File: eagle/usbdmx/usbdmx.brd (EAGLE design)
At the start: 100 x 80 mm, 16 parts, among them IC1 MAX3468CSA, IC2 MAX3468CSA, Q1 16MHz

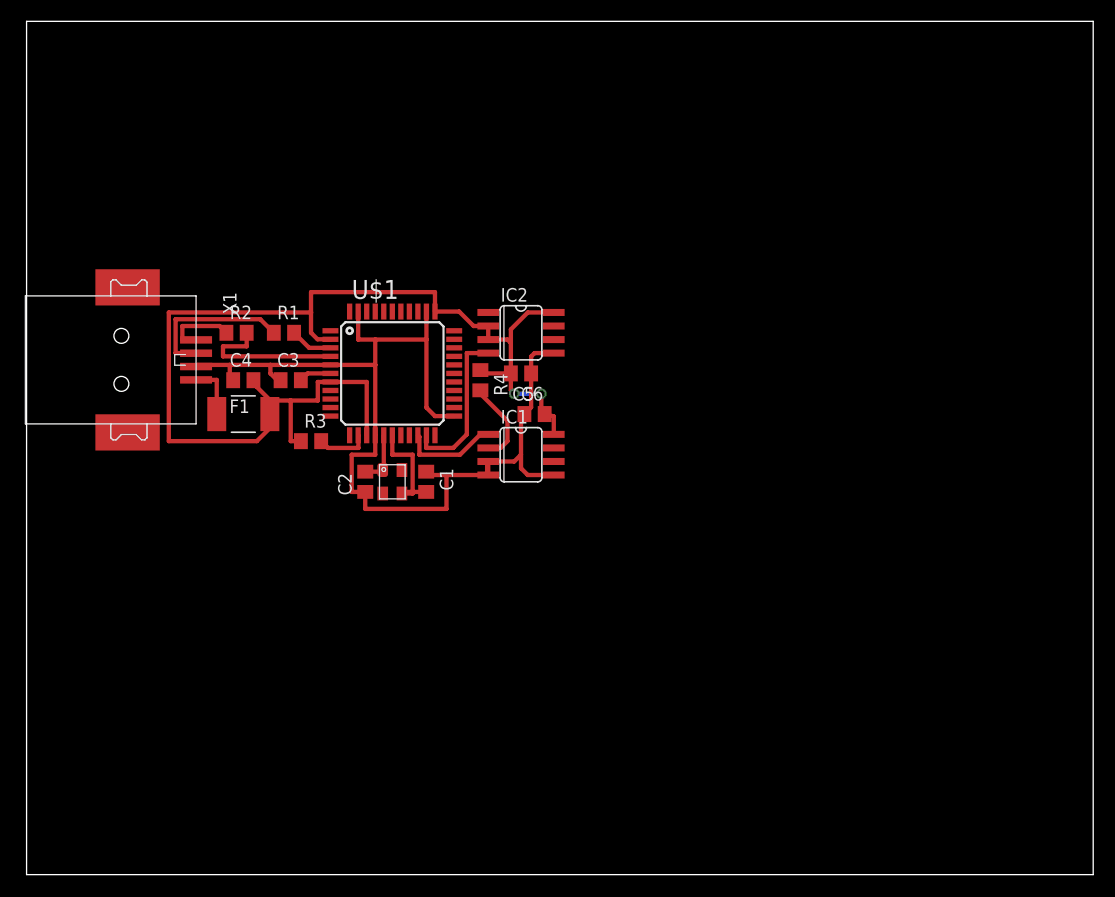
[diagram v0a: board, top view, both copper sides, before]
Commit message: simple layout without galvanic isolation
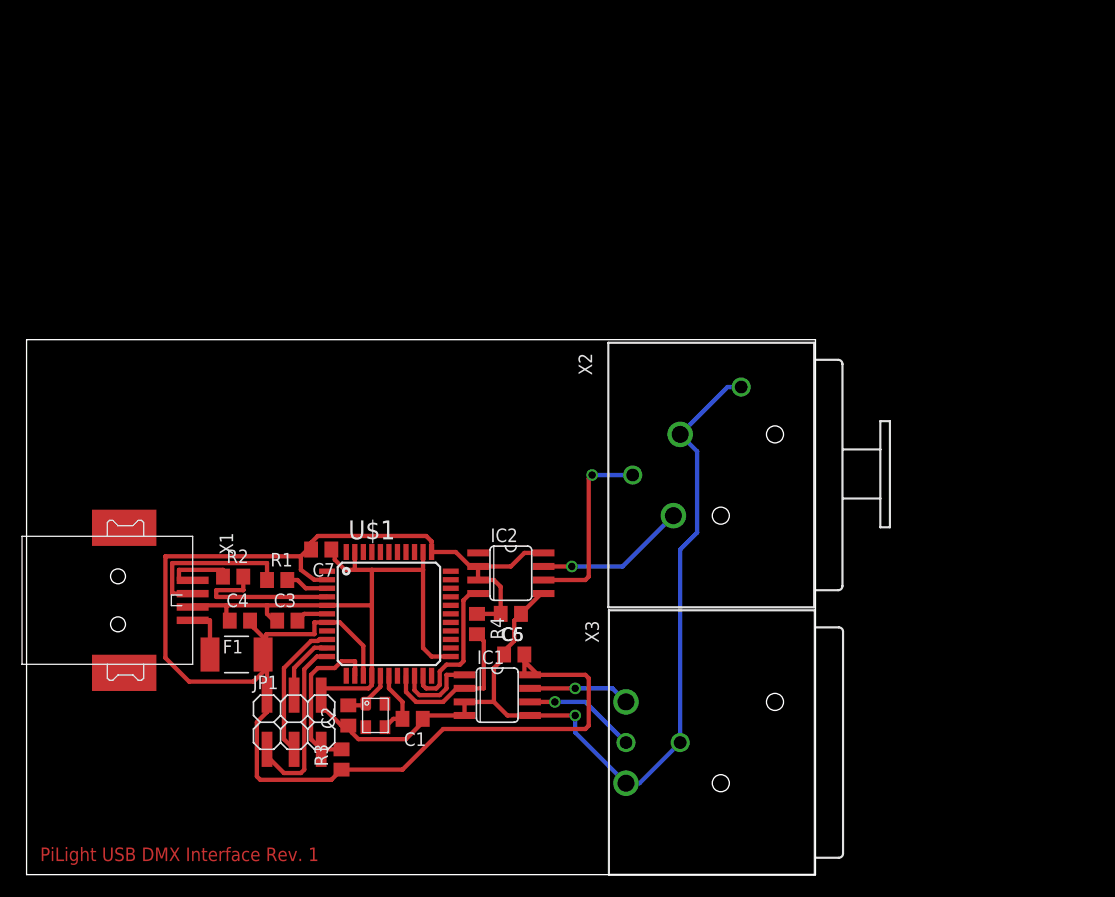
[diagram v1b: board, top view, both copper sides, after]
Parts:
- added C7: (no value), rcl:C0805
- added JP1: (no value), pinhead:2X03SMD
- added X2: NC3FAH2, con-neutrik_ag:NC3FAH2
- added X3: NC3MBH, con-neutrik_ag:NC3MBH
- moved R3 30.0 mm to (29.5, 10.8), turned to 90 degrees
- moved R1 23.2 mm to (23.5, 27.6)
- moved R2 22.9 mm to (19.4, 27.9)
- moved R4 22.9 mm to (42.2, 23.5)
- moved IC1 22.7 mm to (44.1, 16.8)
- moved C6 22.6 mm to (45.7, 20.6)
- moved C5 22.6 mm to (45.4, 24.4)
- moved IC2 22.6 mm to (45.4, 28.3)
- moved F1 22.6 mm to (19.7, 20.6)
- moved U$1 22.5 mm to (34.0, 24.4)
- moved C3 22.5 mm to (24.4, 23.8)
- moved C4 22.5 mm to (20.0, 23.8)
- moved X1 22.5 mm to (8.57, 25.7)
- moved C1 22.3 mm to (36.2, 14.6), turned to 180 degrees
- moved C2 22.0 mm to (30.2, 14.9)
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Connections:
- new net N$13: JP1.1, U$1.11
- new net N$14: JP1.4, U$1.10
- new net N$15: JP1.3, U$1.9
- new net N$16: IC1.2, R4.2, U$1.19
- new net N$17: IC2.7, X2.2
- new net N$18: IC1.6, X3.3
- new net N$19: IC1.7, X3.2
- net GND: now also C7.1, JP1.6, X2.1, X2.G, X3.1, X3.G
- net N$12: now also IC2.6, X2.3; no longer IC1.2, R4.2
- net N$9: now also JP1.5
- net VCC: now also C7.2, JP1.2
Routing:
- net GND: track 100.3 -> 154.4 mm, vias 0 -> 1
- net VCC: track 111.9 -> 155.1 mm, vias 2 -> 0
- net N$13: track 0.00 -> 17.6 mm
- net N$16: track 0.00 -> 15.1 mm
- net N$17: track 0.00 -> 14.1 mm, vias 0 -> 1
- net N$15: track 0.00 -> 13.2 mm
- net N$9: track 4.97 -> 16.6 mm
- net N$18: track 0.00 -> 10.6 mm, vias 0 -> 1
- net N$12: track 7.88 -> 17.8 mm, vias 0 -> 1
- net N$19: track 0.00 -> 9.52 mm, vias 0 -> 1
- net N$14: track 0.00 -> 6.43 mm
- net N$1: track 10.8 -> 6.54 mm
- net N$11: track 9.12 -> 7.77 mm
- net N$10: track 15.2 -> 13.9 mm
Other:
- board size 100 x 80 mm -> 74 x 50.2 mm
- board text added: "PiLight USB DMX Interface Rev. 1"

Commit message: complete design with optocouplers and dc-dc-transformer for galvanic isolation
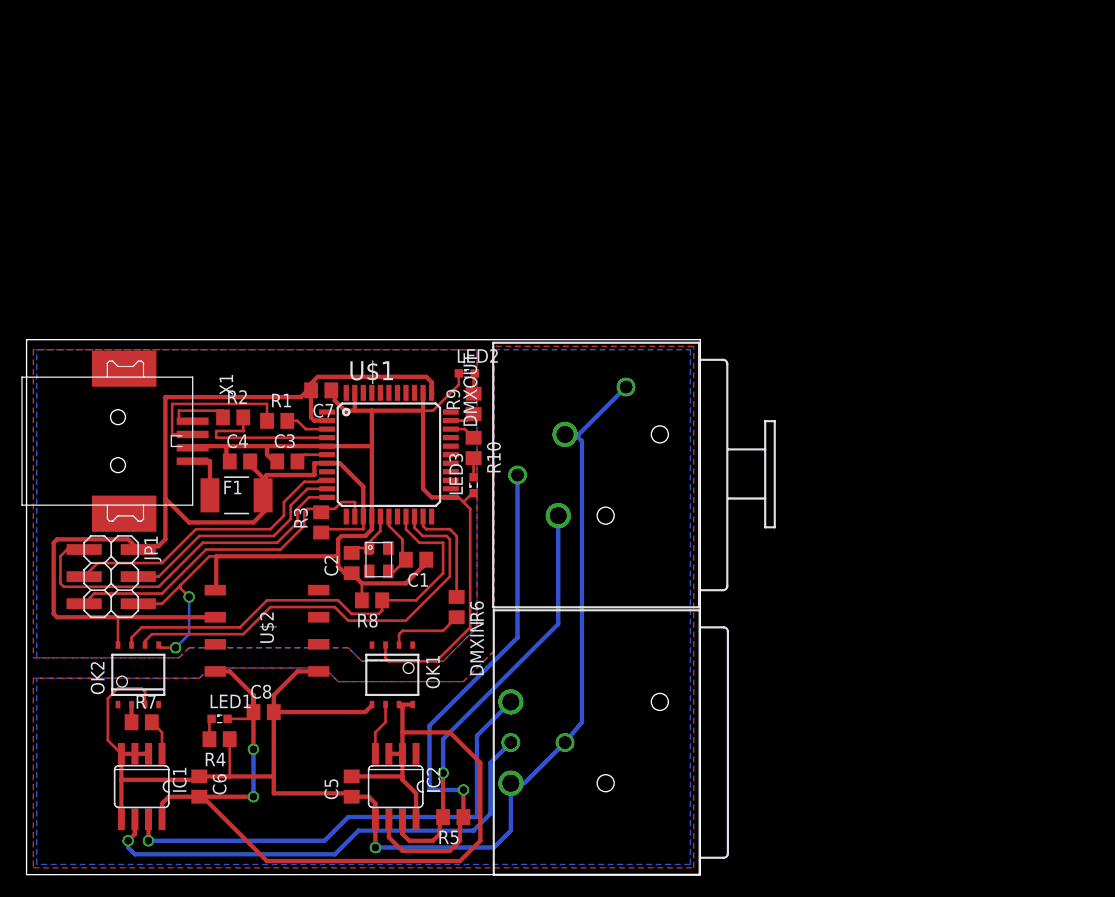
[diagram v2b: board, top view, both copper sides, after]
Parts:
- removed X2: NC3FAH2, con-neutrik_ag:NC3FAH2
- removed X3: NC3MBH, con-neutrik_ag:NC3MBH
- added C8: (no value), rcl:C0805
- added DMXIN: NC3MBH, con-neutrik_ag:NC3MBH
- added DMXOUT: NC3FAH2, con-neutrik_ag:NC3FAH2
- added LED1, LED2, LED3: (no value), led:SML0603
- added OK1, OK2: 6N137SO-8, optocoupler:SO-8
- added R10, R9: 220, rcl:R0805
- added R5: 120, rcl:R0805
- added R6, R7: 470, rcl:R0805
- added R8: 10k, rcl:R0805
- added U$2: NTE0505SNTE0505MEC, murata-dcdc:SMT
- C3: value (none) -> 1µ
- JP1: value (none) -> ICSP
- R4: value (none) -> 220
- moved IC1 34.4 mm to (10.8, 8.26), turned to 180 degrees
- moved C6 32.0 mm to (16.2, 8.26), turned to 270 degrees
- moved R4 26.4 mm to (18.1, 12.7), turned to 180 degrees
- moved IC2 22.7 mm to (34.6, 8.26), turned to 180 degrees
- moved R3 22.3 mm to (27.6, 33.0)
- moved C5 22.0 mm to (30.5, 8.26), turned to 90 degrees
- moved JP1 20.0 mm to (9.21, 29.2), turned to 270 degrees
- moved C1 14.9 mm to (36.5, 29.5)
- moved C7 14.9 mm to (27.6, 45.4)
- moved F1 14.9 mm to (19.7, 35.6)
- moved R1 14.9 mm to (23.5, 42.5)
- moved C3 14.9 mm to (24.4, 38.7)
- moved C4 14.9 mm to (20.0, 38.7)
- moved X1 14.9 mm to (8.57, 40.6)
- moved R2 14.9 mm to (19.4, 42.9)
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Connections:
- new net N$20: IC2.4, OK1.6
- new net N$21: IC1.1, R7.2
- new net N$22: LED3.A, R10.2
- new net N$23: OK2.2, R7.1
- new net N$24: OK2.6, U$1.20
- new net N$25: OK1.2, R6.2
- new net N$26: LED2.A, R9.2
- new net N$27: R9.1, U$1.32
- new net N$28: R10.1, U$1.31
- new net SGND: C5.1, C6.1, C8.2, DMXIN.1, DMXIN.G, DMXOUT.1, DMXOUT.G, IC1.2, IC1.3, IC1.4, IC1.5, IC2.5, OK1.5, OK2.3, R4.1, U$2.8
- new net SVCC: C5.2, C6.2, C8.1, IC1.8, IC2.2, IC2.3, IC2.8, LED1.A, OK1.7, OK1.8, U$2.7
- net GND: now also LED2.C, LED3.C, OK1.3, OK2.5, R8.2, U$2.1; no longer C5.1, C6.1, IC1.3, IC1.4, IC1.5, IC2.5, X2.1, X2.G, X3.1, X3.G
- net N$10: now also R6.1; no longer IC2.4
- net N$11: now also LED1.C, R4.2; no longer IC1.1, U$1.20
- net N$12: now also DMXOUT.3, R5.1; no longer X2.3
- net N$16: now also OK2.7, R8.1; no longer IC1.2, R4.2
- net N$17: now also DMXOUT.2, R5.2; no longer X2.2
- net N$18: now also DMXIN.3; no longer X3.3
- net N$19: now also DMXIN.2; no longer X3.2
- net VCC: now also OK2.8, U$2.3; no longer C5.2, C6.2, IC1.8, IC2.2, IC2.3, IC2.8, R4.1
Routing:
- net SGND: track 0.00 -> 137.7 mm, vias 0 -> 1
- net SVCC: track 0.00 -> 92.5 mm, vias 0 -> 2
- net N$24: track 0.00 -> 40.8 mm
- net N$19: track 9.52 -> 45.8 mm
- net N$18: track 10.6 -> 46.2 mm
- net VCC: track 155.1 -> 120.4 mm
- net N$12: track 17.8 -> 50.3 mm
- net N$16: track 15.1 -> 42.1 mm
- net N$17: track 14.1 -> 39.8 mm
- net GND: track 154.4 -> 136.0 mm, vias 1 -> 2
- net N$13: track 17.6 -> 34.4 mm
- net N$14: track 6.43 -> 22.7 mm
- net N$9: track 16.6 -> 31.7 mm
- net N$15: track 13.2 -> 27.3 mm
- net N$25: track 0.00 -> 7.08 mm
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- added copper zone on layer 1, net GND
- added copper zone on layer 16, net GND
- added copper zone on layer 1, net SGND
- added copper zone on layer 16, net SGND
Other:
- board size 74 x 50.2 mm -> 63.2 x 50.2 mm
- board text removed: "PiLight USB DMX Interface Rev. 1"

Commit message: fix minor errors
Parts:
- C4, C5, C6, C7: value (none) -> 100n
- C8: value (none) -> 4,7µ
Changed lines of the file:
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@@
 <element name="U$1" library="adafruit" package="TQFP44" value="ATMEGA32U4-AU" x="33.9725" y="39.37"/>
 <element name="X1" library="con-usb-3" package="USB-B-SMT" value="" x="8.5725" y="40.64"/>
-<element name="C4" library="rcl" package="C0805" value="" x="20.0025" y="38.735"/>
-<element name="C5" library="rcl" package="C0805" value="" x="30.48" y="8.255" rot="R90"/>
-<element name="C6" library="rcl" package="C0805" value="" x="16.1925" y="8.255" rot="R270"/>
+<element name="C4" library="rcl" package="C0805" value="100n" x="20.0025" y="38.735"/>
+<element name="C5" library="rcl" package="C0805" value="100n" x="30.48" y="8.255" rot="R90"/>
+<element name="C6" library="rcl" package="C0805" value="100n" x="16.1925" y="8.255" rot="R270"/>
 <element name="JP1" library="pinhead" package="2X03SMD" value="ICSP" x="9.2075" y="29.21" rot="R270"/>
-<element name="C7" library="rcl" package="C0805" value="" x="27.6225" y="45.4025" rot="R180"/>
+<element name="C7" library="rcl" package="C0805" value="100n" x="27.6225" y="45.4025" rot="R180"/>
 <element name="DMXOUT" library="con-neutrik_ag" package="NC3FAH2" value="NC3FAH2" x="49.8475" y="37.465" rot="R270">
 <attribute name="OC_NEWARK" value="27B4208" x="49.8475" y="37.465" size="1.778" layer="27" rot="R270" display="off"/>
@@
 </element>
 <element name="U$2" library="murata-dcdc" package="SMT" value="NTE0505SNTE0505MEC" x="22.5425" y="22.86"/>
-<element name="C8" library="rcl" package="C0805" value="" x="22.225" y="15.24"/>
+<element name="C8" library="rcl" package="C0805" value="4,7µ" x="22.225" y="15.24"/>
 <element name="R5" library="rcl" package="R0805" value="120" x="40.005" y="5.3975" rot="R180"/>
 <element name="OK1" library="optocoupler" package="SO-8" value="6N137SO-8" x="34.29" y="18.7325" rot="R270"/>
@@
 <contactref element="DMXOUT" pad="1"/>
 <contactref element="DMXOUT" pad="G"/>
-<contactref element="U$2" pad="8"/>
-<contactref element="C8" pad="2"/>
 <contactref element="C5" pad="1"/>
-<wire x1="27.3925" y1="19.05" x2="25.4" y2="19.05" width="0.4064" layer="1"/>
-<wire x1="25.4" y1="19.05" x2="23.1775" y2="16.8275" width="0.4064" layer="1"/>
-<wire x1="23.1775" y1="16.8275" x2="23.1775" y2="16.83" width="0.4064" layer="1"/>
-<wire x1="23.1775" y1="16.83" x2="23.175" y2="15.24" width="0.4064" layer="1"/>
 <contactref element="OK1" pad="5"/>
 <contactref element="OK2" pad="3"/>
-<wire x1="23.175" y1="15.24" x2="31.75" y2="15.24" width="0.4064" layer="1"/>
 <wire x1="31.75" y1="15.24" x2="32.385" y2="15.875" width="0.4064" layer="1"/>
 <wire x1="32.385" y1="15.875" x2="32.385" y2="15.9425" width="0.4064" layer="1"/>
 <wire x1="30.48" y1="7.305" x2="30.165" y2="7.62" width="0.4064" layer="1"/>
 <wire x1="30.165" y1="7.62" x2="23.175" y2="7.62" width="0.4064" layer="1"/>
-<wire x1="23.175" y1="9.205" x2="23.175" y2="15.24" width="0.4064" layer="1"/>
 <wire x1="51.435" y1="41.275" x2="51.7625" y2="41.275" width="0.4064" layer="16"/>
 <wire x1="51.7625" y1="41.275" x2="56.2025" y2="45.715" width="0.4064" layer="16"/>
@@
 <contactref element="IC1" pad="2"/>
 <wire x1="10.16" y1="11.3284" x2="11.43" y2="11.3284" width="0.4064" layer="1"/>
-<contactref element="R4" pad="1"/>
-<wire x1="19.0475" y1="12.7" x2="19.05" y2="12.7" width="0.254" layer="1"/>
 <wire x1="19.05" y1="12.7" x2="19.05" y2="9.205" width="0.254" layer="1"/>
 <polygon width="0.4064" layer="1" isolate="0.6096" orphans="yes">
@@
 <vertex x="0.9525" y="0.9525"/>
 </polygon>
+<contactref element="R4" pad="1"/>
+<contactref element="C8" pad="2"/>
+<contactref element="U$2" pad="8"/>
+<wire x1="27.3925" y1="19.05" x2="25.4" y2="19.05" width="0.4064" layer="1"/>
+<wire x1="25.4" y1="19.05" x2="23.1775" y2="16.8275" width="0.4064" layer="1"/>
+<wire x1="23.1775" y1="16.8275" x2="23.1775" y2="15.2425" width="0.4064" layer="1"/>
+<wire x1="23.1775" y1="15.2425" x2="23.175" y2="15.24" width="0.4064" layer="1"/>
+<wire x1="23.175" y1="15.24" x2="23.175" y2="9.205" width="0.4064" layer="1"/>
+<wire x1="31.75" y1="15.24" x2="23.175" y2="15.24" width="0.4064" layer="1"/>
 </signal>
 <signal name="N$20">
